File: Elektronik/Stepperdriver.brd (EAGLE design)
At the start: 100 x 100 mm, 27 parts

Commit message: Elektronik auf den neusten Stand gebracht (Merge mit privater Dropbox
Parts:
- removed ADDR_A, ADDR_B, STPCLK_A, STPCLK_B: 219-10, switch-dil:CTS-219-10
- added ADDA, ADDB, SCLKA, SCLKB: 219-08, switch-dil:CTS-219-08
- added C10, C5: 100µ, rcl:150CLZ-1010
- added C11, C6: 220n, rcl:C0805
- added C12, C7, C8, C9: 100n, rcl:C0805
- added C_REGA, C_REGB: 22µ, rcl:C0805
- added R4, R5: 1k, rcl:R0805
- added R6, R7: 1M, rcl:R0805
- C2, C4: value 10n -> 220n
- H1, H2, H3, H4: value MOUNT-HOLE5.0 -> MOUNT-PAD-ROUND5.0; device holes:5,0 -> holes:5,0-PAD
- moved R3 119.5 mm to (76.8, 58.1), turned to 90 degrees
- moved R2 118.2 mm to (79.1, 58.1), turned to 90 degrees
- moved R1 117.1 mm to (81.3, 58.1), turned to 90 degrees
- moved FAULT 107.4 mm to (76.2, 54.3), turned to 180 degrees
- moved B_BUSY 105.1 mm to (80.0, 54.0), turned to 180 degrees
- moved A_BUSY 101.6 mm to (82.2, 54.0)
- moved C2 32.5 mm to (43.5, 42.9), turned to 90 degrees
- moved C1 32.0 mm to (46.0, 42.9), turned to 90 degrees
- moved D1 28.9 mm to (43.2, 46.7), turned to 270 degrees
- moved C3 26.4 mm to (71.4, 43.2), turned to 90 degrees
- moved D2 20.6 mm to (68.9, 47.0), turned to 270 degrees
- moved C4 20.1 mm to (68.9, 43.2), turned to 90 degrees
- moved U$1 17.2 mm to (47.3, 29.5), turned to 270 degrees
- moved U$2 5.41 mm to (72.7, 29.5), turned to 270 degrees
- turned SV1 to 270 degrees
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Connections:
- net N$101 renamed IO113
- net N$102 renamed IO111
- net N$103 renamed IO109
- net N$104 renamed IO107
- net N$105 renamed IO105
- net N$106 renamed IO103
- net N$107 renamed IO101
- net N$108 renamed IO99
- net N$109 renamed IO97
- net N$110 renamed IO95
- net N$111 renamed IO93
- net N$112 renamed IO91
- net N$113 renamed IO89
- net N$114 renamed IO87
- net N$115 renamed IO85
- net N$116 renamed IO83
- net N$117 renamed IO81
- net N$118 renamed IO79
- net N$119 renamed IO77
- net N$12 renamed IO16
- net N$120 renamed IO75
- net N$121 renamed IO54
- net N$122 renamed IO56
- net N$123 renamed IO58
- net N$124 renamed IO60
- net N$125 renamed IO62
- net N$126 renamed IO64
- net N$127 renamed IO66
- net N$128 renamed IO68
- net N$129 renamed IO70
- net N$13 renamed IO18
- net N$130 renamed IO72
- net N$131 renamed IO55
- net N$132 renamed IO57
- net N$133 renamed IO59
- net N$134 renamed IO61
- net N$135 renamed IO63
- net N$136 renamed IO65
- net N$137 renamed IO67
- net N$138 renamed IO69
- net N$139 renamed IO71
- net N$14 renamed IO20
- net N$140 renamed IO73
- net N$141 renamed IO35
- net N$142 renamed IO37
- net N$143 renamed IO39
- net N$144 renamed IO41
- net N$145 renamed IO43
- net N$146 renamed IO45
- net N$147 renamed IO47
- net N$148 renamed IO49
- net N$149 renamed IO51
- net N$15 renamed IO22
- net N$150 renamed IO53
- net N$151 renamed IO34
- net N$152 renamed IO36
- net N$153 renamed IO38
- net N$154 renamed IO40
- net N$155 renamed IO42
- net N$156 renamed IO44
- net N$157 renamed IO46
- net N$158 renamed IO48
- net N$159 renamed IO50
- net N$16 renamed IO24
- net N$160 renamed IO52
- net N$17 renamed IO26
- net N$18 renamed IO28
- net N$19 renamed IO30
- net N$20 renamed IO32
- net N$32 renamed IO17
- net N$33 renamed IO19
- net N$34 renamed IO21
- net N$35 renamed IO23
- net N$36 renamed IO25
- net N$37 renamed IO27
- net N$38 renamed IO29
- net N$39 renamed IO31
- net N$40 renamed IO33
- net N$41 renamed IO74
- net N$42 renamed IO76
- net N$43 renamed IO78
- net N$44 renamed IO80
- net N$45 renamed IO82
- net N$46 renamed IO84
- net N$47 renamed IO86
- net N$48 renamed IO88
- net N$49 renamed IO90
- net N$50 renamed IO92
- net N$51 renamed IO94
- net N$52 renamed IO96
- net N$53 renamed IO98
- net N$54 renamed IO100
- net N$55 renamed IO102
- net N$56 renamed IO104
- net N$57 renamed IO106
- net N$58 renamed IO108
- net N$59 renamed IO110
- net N$60 renamed IO112
- removed net N$10: SV2.20
- removed net N$11: SV2.22
- removed net N$21: SV2.1
- removed net N$22: SV2.3
- removed net N$23: SV2.5
- removed net N$24: SV2.7
- removed net N$25: SV2.9
- removed net N$26: SV2.11
- removed net N$27: SV2.13
- removed net N$28: SV2.15
- removed net N$29: SV2.17
- removed net N$30: SV2.19
- removed net N$31: SV2.21
- removed net N$64: U$2.20, U$2.21, X1.8
- removed net N$65: U$2.17, U$2.18, X1.9
- removed net N$69: U$1.2, U$1.3, X1.3
- removed net N$7 (its old number): SV2.14
- removed net N$70: U$1.35, U$1.36, X1.4
- removed net N$72: U$1.17, U$1.18, X1.5
- removed net N$73: U$1.20, U$1.21, X1.6
- removed net N$79: A_BUSY.C
- removed net N$8 (its old number): SV2.16
- removed net N$80: B_BUSY.C
- removed net N$81: FAULT.C
- removed net N$85: ADDR_A.1, ADDR_B.1, STPCLK_A.1, STPCLK_B.1
- removed net N$86: ADDR_A.2, ADDR_B.2, STPCLK_A.2, STPCLK_B.2
- removed net N$87: ADDR_A.3, ADDR_B.3, STPCLK_A.3, STPCLK_B.3
- removed net N$88: ADDR_A.4, ADDR_B.4, STPCLK_A.4, STPCLK_B.4
- removed net N$89: ADDR_A.5, ADDR_B.5, STPCLK_A.5, STPCLK_B.5
- removed net N$9: SV2.18
- removed net N$90: ADDR_A.6, ADDR_B.6, STPCLK_A.6, STPCLK_B.6
- removed net N$91: ADDR_A.7, ADDR_B.7, STPCLK_A.7, STPCLK_B.7
- removed net N$92: ADDR_A.8, ADDR_B.8, STPCLK_A.8, STPCLK_B.8
- removed net N$93: ADDR_A.9, ADDR_B.9, STPCLK_A.9, STPCLK_B.9
- removed net N$94: ADDR_A.10, ADDR_B.10, STPCLK_A.10, STPCLK_B.10
- removed net SW_A: U$1.7, X1.7
- new net IO0: ADDA.1, ADDB.1, SV2.8
- new net IO1: ADDA.2, ADDB.2, SV2.7
- new net IO10: SCLKA.3, SCLKB.3, SV2.18
- new net IO11: SCLKA.4, SCLKB.4, SV2.17
- new net IO12: SCLKA.5, SCLKB.5, SV2.20
- new net IO13: SCLKA.6, SCLKB.6, SV2.19
- new net IO14: SCLKA.7, SCLKB.7, SV2.22
- new net IO15: SCLKA.8, SCLKB.8, SV2.21
- new net IO2: ADDA.3, ADDB.3, SV2.10
- new net IO3: ADDA.4, ADDB.4, SV2.9
- new net IO4: ADDA.5, ADDB.5, SV2.12
- new net IO5: ADDA.6, ADDB.6, SV2.11
- new net IO6: ADDA.7, ADDB.7, SV2.14
- new net IO7: ADDA.8, ADDB.8, SV2.13
- new net IO8: SCLKA.1, SCLKB.1, SV2.16
- new net IO9: SCLKA.2, SCLKB.2, SV2.15
- new net N$82: C9.1, R5.2, R7.1, U$2.7
- new net N$83: C8.1, R4.2, R6.1, U$1.7
- new net N$84: R4.1, X1.7
- net !CS_A: now also ADDA.10, ADDA.11, ADDA.12, ADDA.13, ADDA.14, ADDA.15, ADDA.16, ADDA.9; no longer ADDR_A.11, ADDR_A.12, ADDR_A.13, ADDR_A.14, ADDR_A.15, ADDR_A.16, ADDR_A.17, ADDR_A.18, ADDR_A.19, ADDR_A.20
- net !CS_B: now also ADDB.10, ADDB.11, ADDB.12, ADDB.13, ADDB.14, ADDB.15, ADDB.16, ADDB.9; no longer ADDR_B.11, ADDR_B.12, ADDR_B.13, ADDR_B.14, ADDR_B.15, ADDR_B.16, ADDR_B.17, ADDR_B.18, ADDR_B.19, ADDR_B.20
- net !FLAG: now also FAULT.C
- net +3V3: now also C12.1, C7.1, C_REGA.1, C_REGB.1, SV2.2, SV2.4, SV2.6
- net BUSY_A: now also A_BUSY.C
- net BUSY_B: now also B_BUSY.C
- net GND: now also C10.-, C11.2, C12.2, C5.-, C6.2, C7.2, C8.2, C9.2, C_REGA.2, C_REGB.2, H1.B5, H2.B5, H3.B5, H4.B5, R6.2, R7.2, SV2.1, SV2.3, SV2.5
- net N$1: now also U$1.2, U$1.3, X1.6; no longer SV2.2
- net N$2: now also U$1.35, U$1.36, X1.5; no longer SV2.4
- net N$3: now also U$1.17, U$1.18, X1.3; no longer SV2.6
- net N$4: now also U$1.20, U$1.21, X1.4; no longer SV2.8
- net N$5: now also U$2.20, U$2.21, X1.9; no longer SV2.10
- net N$6: now also U$2.17, U$2.18, X1.8; no longer SV2.12
- net N$76: now also R5.1; no longer U$2.7
- net STEPCLOCK_A: now also SCLKA.10, SCLKA.11, SCLKA.12, SCLKA.13, SCLKA.14, SCLKA.15, SCLKA.16, SCLKA.9; no longer STPCLK_A.11, STPCLK_A.12, STPCLK_A.13, STPCLK_A.14, STPCLK_A.15, STPCLK_A.16, STPCLK_A.17, STPCLK_A.18, STPCLK_A.19, STPCLK_A.20
- net STEPCLOCK_B: now also SCLKB.10, SCLKB.11, SCLKB.12, SCLKB.13, SCLKB.14, SCLKB.15, SCLKB.16, SCLKB.9; no longer STPCLK_B.11, STPCLK_B.12, STPCLK_B.13, STPCLK_B.14, STPCLK_B.15, STPCLK_B.16, STPCLK_B.17, STPCLK_B.18, STPCLK_B.19, STPCLK_B.20
- net V+: now also C10.+, C11.1, C5.+, C6.1
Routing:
- net IO0: track 0.00 -> 106.3 mm, vias 0 -> 3
- net IO1: track 0.00 -> 105.9 mm, vias 0 -> 3
- net IO2: track 0.00 -> 99.6 mm, vias 0 -> 3
- net IO3: track 0.00 -> 99.4 mm, vias 0 -> 3
- net IO4: track 0.00 -> 93.2 mm, vias 0 -> 3
- net IO5: track 0.00 -> 92.9 mm, vias 0 -> 3
- net IO6: track 0.00 -> 86.7 mm, vias 0 -> 3
- net IO7: track 0.00 -> 86.5 mm, vias 0 -> 3
- net IO8: track 0.00 -> 65.2 mm, vias 0 -> 3
- net IO9: track 0.00 -> 64.9 mm, vias 0 -> 3
- net IO10: track 0.00 -> 58.6 mm, vias 0 -> 3
- net IO11: track 0.00 -> 58.5 mm, vias 0 -> 3
- net N$1: track 0.00 -> 53.0 mm, vias 0 -> 2
- net IO12: track 0.00 -> 52.1 mm, vias 0 -> 3
- net IO13: track 0.00 -> 52.0 mm, vias 0 -> 3
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- added copper zone on layer 1, net GND
- added copper zone on layer 16, net GND

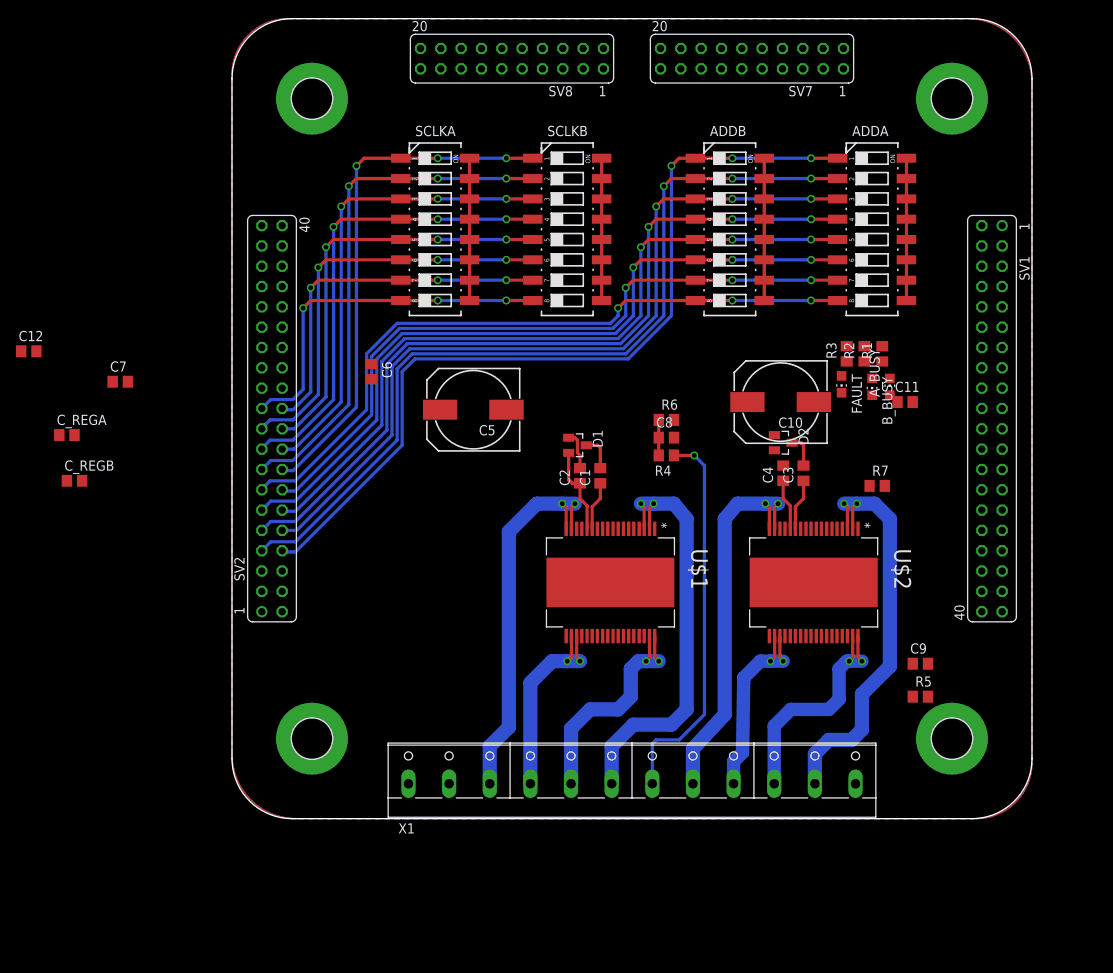
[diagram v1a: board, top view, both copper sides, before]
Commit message: Stepperendstufe weitergeroutet
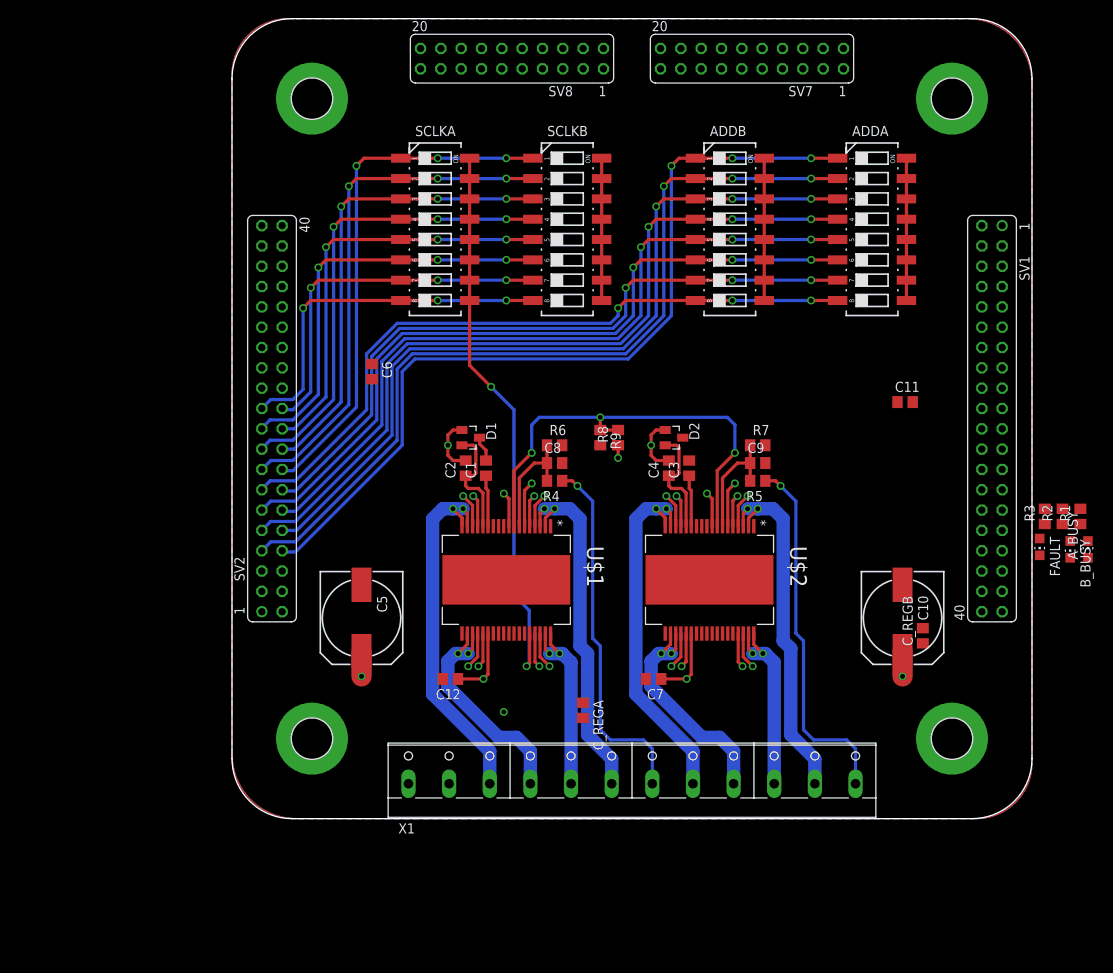
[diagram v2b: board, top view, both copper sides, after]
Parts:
- added R8, R9: 1M, rcl:R0805
- moved C_REGB 107.8 mm to (86.4, 22.9), turned to 90 degrees
- moved C7 76.3 mm to (52.7, 17.5), turned to 180 degrees
- moved C_REGA 73.1 mm to (43.9, 13.5), turned to 270 degrees
- moved C12 66.7 mm to (27.3, 17.5), turned to 180 degrees
- moved R5 33.8 mm to (65.7, 42.2), turned to 180 degrees
- moved C9 32.3 mm to (65.7, 44.5)
- moved A_BUSY 32.0 mm to (107.0, 33.7)
- moved B_BUSY 32.0 mm to (104.8, 33.7)
- moved FAULT 32.0 mm to (101.0, 34.0)
- moved R1 32.0 mm to (106.0, 37.8)
- moved R2 32.0 mm to (103.8, 37.8)
- moved R3 32.0 mm to (101.6, 37.8)
- moved C10 31.0 mm to (83.8, 25.1), turned to 270 degrees
- moved C5 29.5 mm to (16.2, 25.1), turned to 270 degrees
- moved R7 15.8 mm to (65.7, 46.7)
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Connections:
- net ADCIN: now also R8.2, R9.1
- net GND: now also R9.2
- net V+: now also R8.1
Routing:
- net V+: track 4.86 -> 90.6 mm, vias 0 -> 21
- net ADCIN: track 0.00 -> 57.2 mm, vias 0 -> 3
- net STEPCLOCK_A: track 17.8 -> 71.0 mm, vias 0 -> 2
- net N$76: track 0.00 -> 45.7 mm, vias 0 -> 1
- net +3V3: track 0.00 -> 38.4 mm, vias 0 -> 6
- net N$82: track 0.00 -> 14.7 mm
- net N$83: track 4.44 -> 14.7 mm
- net N$1: track 53.0 -> 44.8 mm
- net N$63: track 6.37 -> 14.4 mm
- net N$8: track 51.8 -> 44.8 mm
- net N$7: track 30.4 -> 24.0 mm
- net N$2: track 30.1 -> 24.0 mm
- net N$62: track 4.11 -> 0.00 mm
- net N$6: track 48.9 -> 45.4 mm
- net N$3: track 48.9 -> 45.4 mm
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- added copper zone on layer 15, net +3V3
- added copper zone on layer 2, net V+
